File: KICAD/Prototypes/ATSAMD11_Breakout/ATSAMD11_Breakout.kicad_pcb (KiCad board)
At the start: 2 copper layers, 47.6 x 33 mm, 21 parts, among them J1 JTAGICE3-10p, SW1 SW_PUSH, U1 ATSAMD11D, U2 USB2, U3 VREG-SOT23, X1 ABS25-32.768KHZ

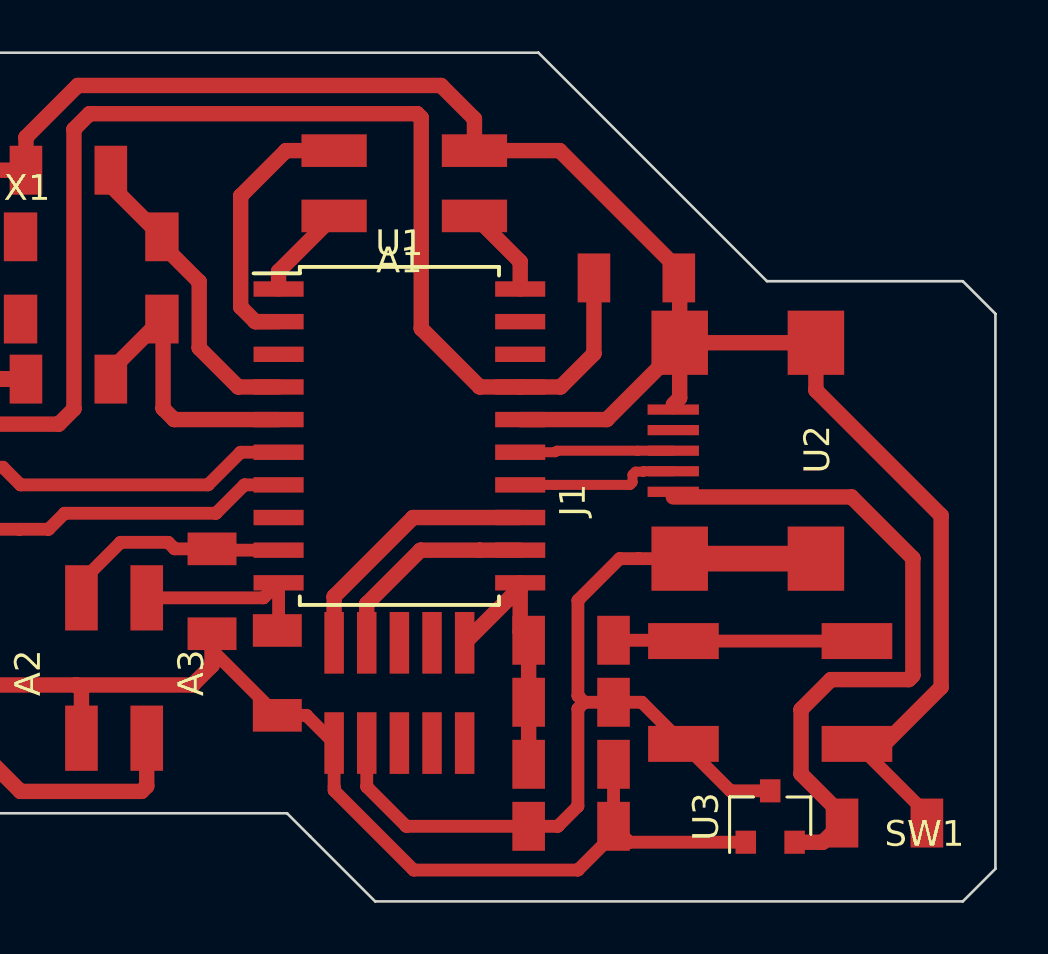
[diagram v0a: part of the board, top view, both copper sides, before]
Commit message: Provided clearance for USB cable
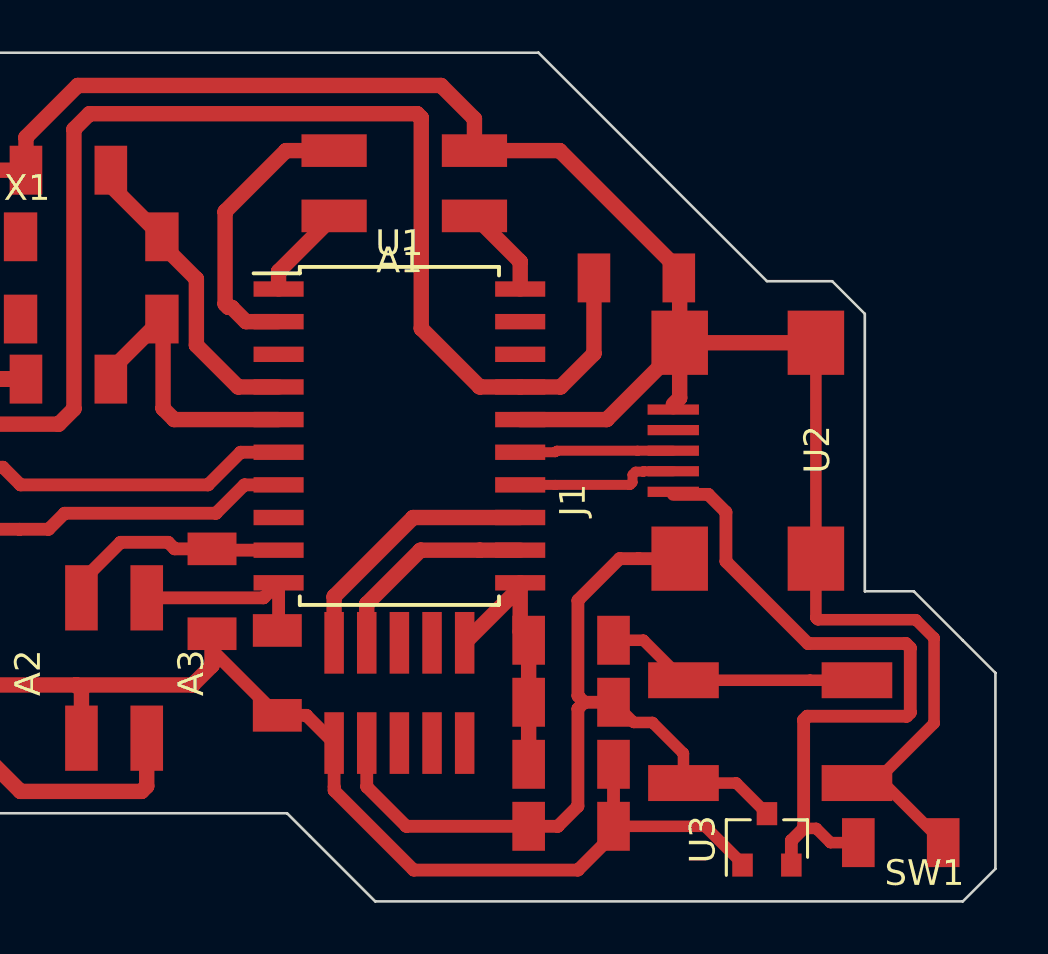
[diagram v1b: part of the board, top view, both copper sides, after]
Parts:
- moved SW1 1.52 mm to (114.4, 111.5)
- moved C6 0.99 mm to (119.5, 115.8)
- moved U3 0.90 mm to (114.3, 115.7)
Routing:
- net GND: track 161.8 -> 160.8 mm
- net Net-(A1-Pad1): track 10.4 -> 11.2 mm
- net Net-(R1-Pad2): track 9.48 -> 10.1 mm
- net VRAW: track 27.2 -> 27.8 mm
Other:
- outline, holes or cut-outs redrawn
- net class Default: clearance 0.39 -> 0.45; trace_width 0.39 -> 0.45
- rule trace_clearance: 0.39 -> 0.45

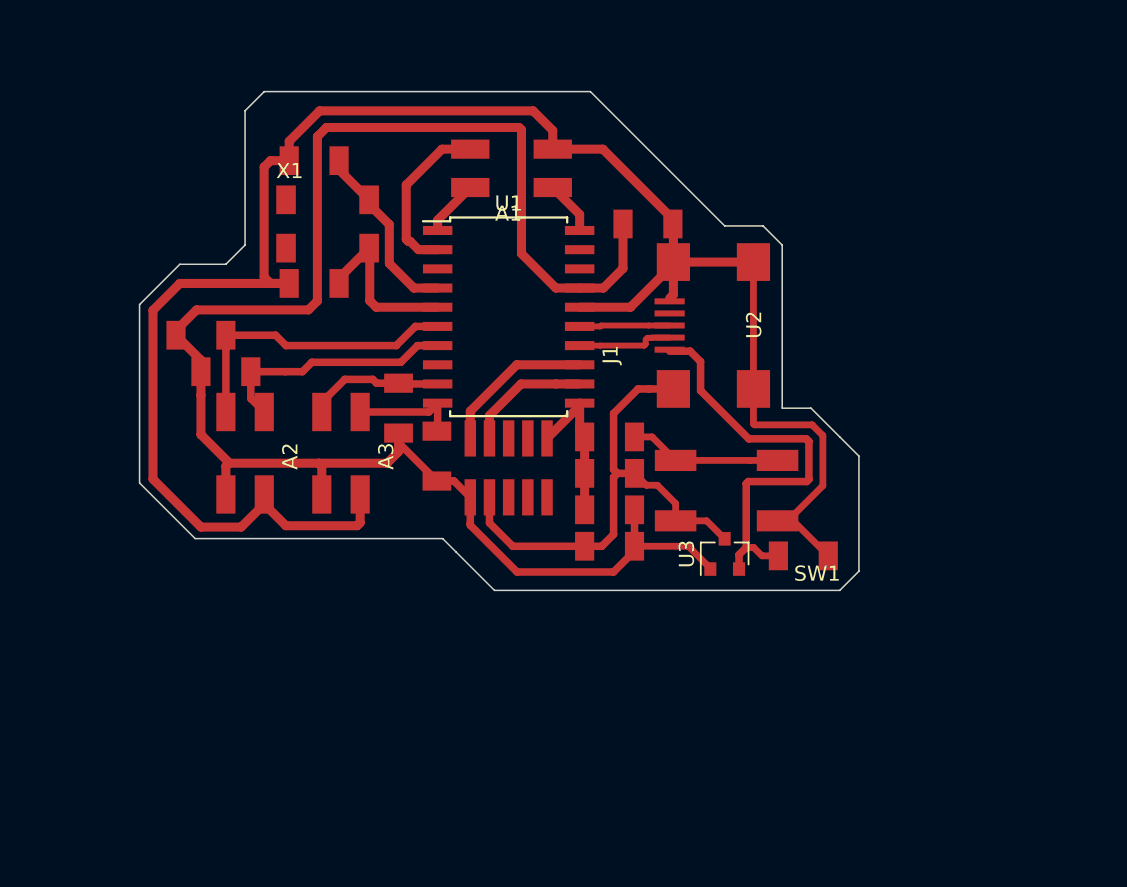
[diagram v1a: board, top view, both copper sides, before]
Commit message: added RTC library, board defs derived from Mattairtech
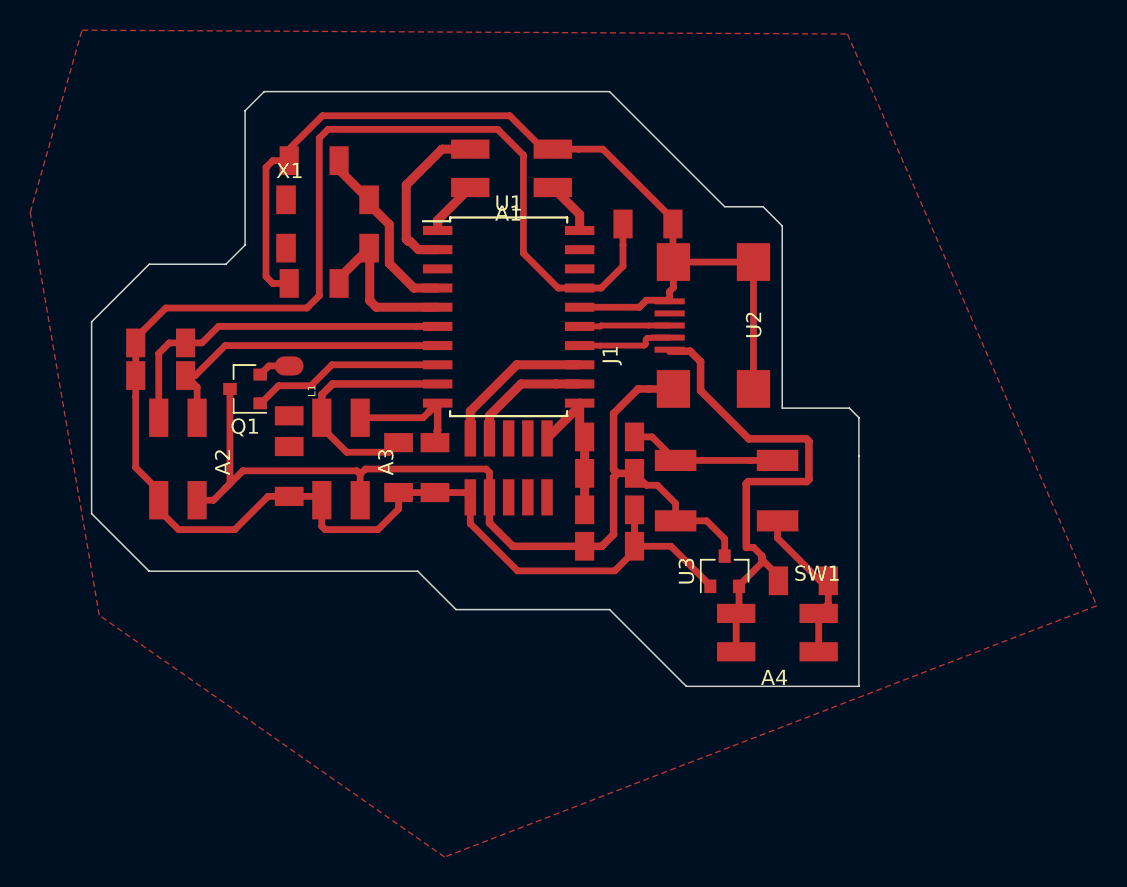
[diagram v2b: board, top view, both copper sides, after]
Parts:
- added A4: APA, _Fab_Footprint:SMD-Header-2x2, F.Cu at (117.6, 120.9)
- added L1: FAB_LED, _Fab_Footprint:LED_1206_FAB, F.Cu at (85.5, 104.9)
- added Q1: N-MOSFET, TO_SOT_Packages_SMD:SOT-23, F.Cu at (82.5, 104.8)
- added R7: RES, _Fab_Footprint:CAP_1206_FAB, F.Cu at (85.5, 110.2)
- moved A2 4.46 mm to (78.1, 109.6)
- moved R6 4.33 mm to (77.0, 103.9)
- moved R3 3.94 mm to (92.7, 110.0)
- moved R5 2.71 mm to (77.0, 101.7)
- moved C6 1.65 mm to (119.5, 117.5)
- moved U3 1.14 mm to (114.3, 116.8)
- moved R4 0.77 mm to (95.1, 110.0)
- moved A3 0.38 mm to (88.9, 109.6)
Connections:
- U1 pad 8: Net-(U1-Pad8) -> EN
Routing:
- net GND: track 160.8 -> 141.4 mm
- net EN: track 0.00 -> 12.8 mm
- net Net-(A3-Pad2): track 9.06 -> 15.8 mm
- net VRAW: track 27.8 -> 34.3 mm
- net +3V3: track 111.4 -> 116.8 mm
- net Net-(A2-Pad4): track 16.1 -> 20.6 mm
- net Net-(A2-Pad2): track 19.9 -> 23.5 mm
- net Net-(L1-Pad2): track 0.00 -> 2.16 mm
- added copper zone on F.Cu, net GND
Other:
- board size 47.6 x 33 mm -> 50.8 x 39.4 mm
